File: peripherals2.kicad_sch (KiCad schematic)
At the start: 0 parts

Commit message: feat: adds the peripherals-2 to project
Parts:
- added C1, C2, C3: 0.1µF, symbol Device:C
- added J1: MSD-4-A, CUI_MSD-4-A, symbol MSD-4-A:MSD-4-A
- added R1, R2, R3, R4, R5, R6, R7, R8, R9: 10k, symbol Device:R
- added U1: GSDA213, LGA12_GAS, symbol GSDA213:GSDA213
- added U2: VEML3235SL, symbol VEML3235SL:BL0937
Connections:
- new net: R7.1, U2.3 (INT)
- new net: C3.2, U1.3 (VDD_IO)
- new net: R8.2, U1.5 (INT1)
- new net: R9.2, U1.6 (INT2)
- new net +3.3V: C1.2, C2.2, J1.1 (DAT2), J1.2 (CD/DAT3), J1.4 (VDD), J1.8 (DAT1), R1.1, R2.1, R3.1, R5.2, R6.2, R7.2, R8.1, R9.1, U1.7 (VDD), U2.1 (VDD), U2.4 (SDA), U2.5 (SCL)
- new net CS: U1.10 (CSB)
- new net GND: C1.1, C2.1, C3.1, J1.6 (VSS), J1.G1 (COVER_GND), J1.G2 (COVER_GND__1), J1.G3 (COVER_GND__2), J1.G4 (COVER_GND__3), R1.2, R2.2, R3.2, R4.2, R5.1, R6.1, U1.8 (GND_IO), U1.9 (GND), U2.2 (GND)
- new net GPIO: J1.CD, R4.1
- new net MISO: J1.7 (DAT0), U1.2 (SDA/SDI/SDO)
- new net MOSI: J1.3 (CMD), U1.1 (SDO/SA0)
- new net SCLK: J1.5 (CLK), U1.12 (SCL/SCLK)

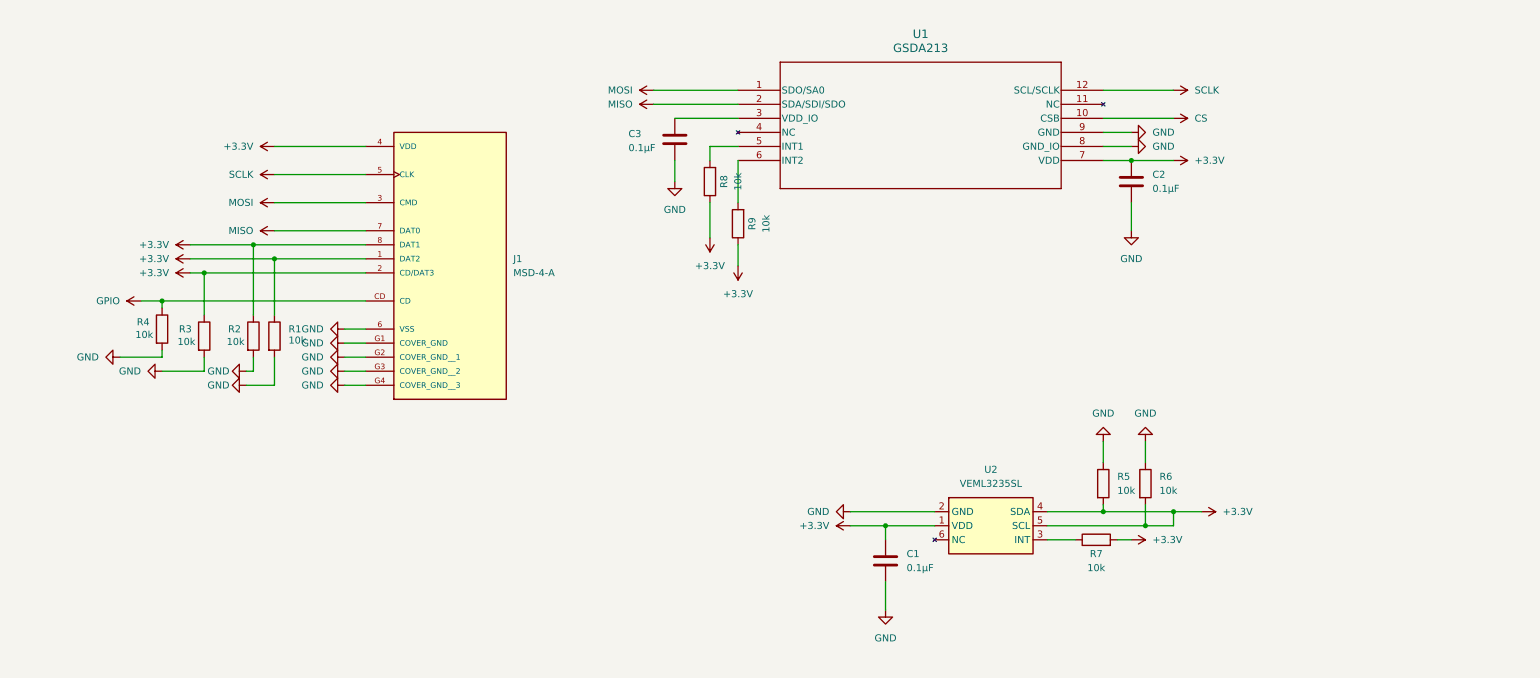
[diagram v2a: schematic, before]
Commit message: refac: adjusts circuits for MicroSD, Accelerometer, Light Sensor
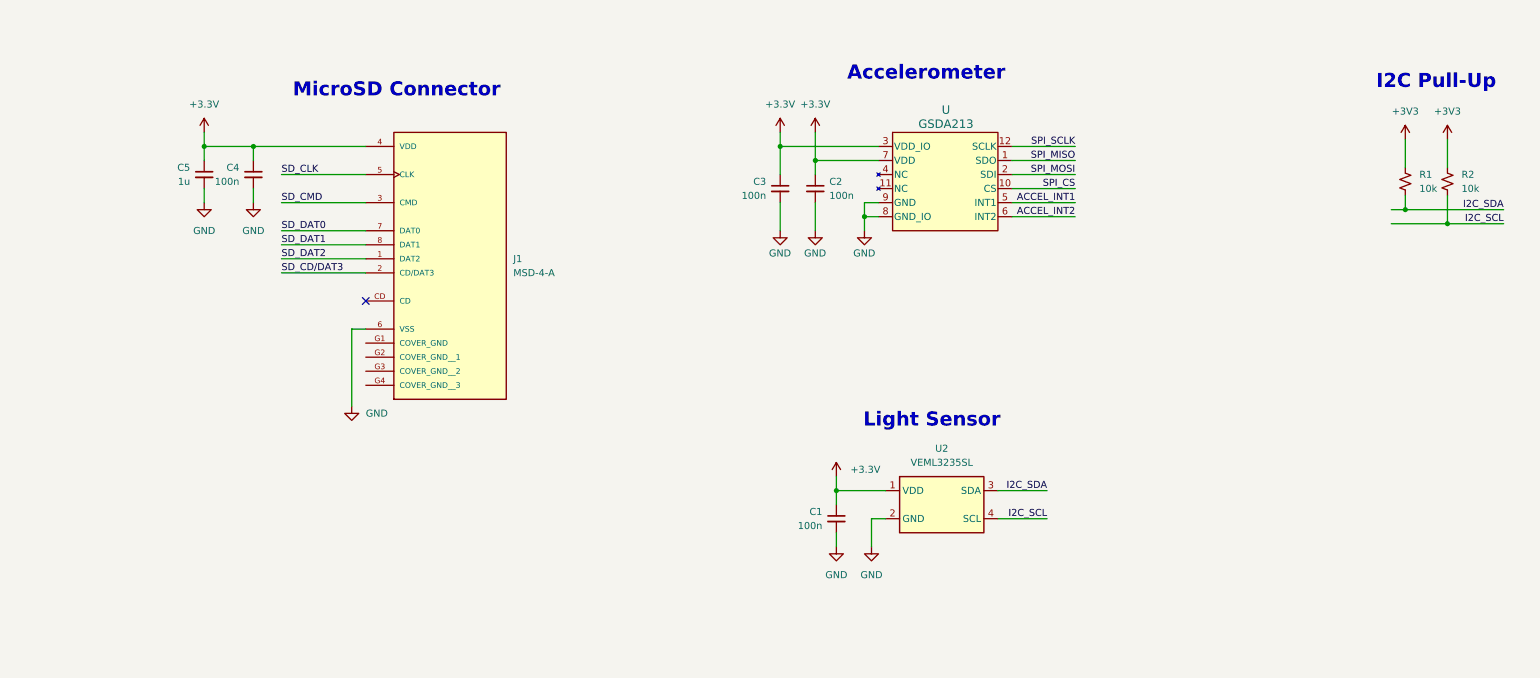
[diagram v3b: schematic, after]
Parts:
- removed C1, C2, C3: 0.1µF, symbol Device:C
- removed R1, R2, R3, R4, R5, R6, R7, R8, R9: 10k, symbol Device:R
- added C1, C2, C3, C4: 100n, symbol Device:C_Small
- added C5: 1u, Capacitor_SMD:C_0402_1005Metric, symbol Device:C_Small
- added R1, R2: 10k, Resistor_SMD:R_0402_1005Metric, symbol Device:R_Small_US
- U: renamed from U1; footprint LGA12_GAS -> (none); MPN (none) -> GSDA213
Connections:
- net +3.3V: now also U.3 (VDD_IO), C1.1, C2.1, C3.1, C4.1, C5.1; no longer J1.1 (DAT2), J1.2 (CD/DAT3), J1.8 (DAT1), U2.4 (SDA), U2.5 (SCL)
- net GND: now also C1.2, C2.2, C3.2, C4.2, C5.2; no longer J1.G1 (COVER_GND), J1.G2 (COVER_GND__1), J1.G3 (COVER_GND__2), J1.G4 (COVER_GND__3)
- net I2C_SDA: now reaches U2.3 (SDA)
- net I2C_SDA: now also R1.2
- net ACCEL_INT1: now reaches U.5 (INT1)
- net ACCEL_INT2: now reaches U.6 (INT2)
- net CS renamed SPI_CS
- net GPIO: no longer names the net of J1.CD
- net MISO renamed SD_DAT0
- net SD_DAT0: no longer U.2 (SDA/SDI/SDO)
- net MOSI renamed SD_CMD
- net SD_CMD: no longer U.1 (SDO/SA0)
- net SCLK renamed SD_CLK
- net SD_CLK: no longer U.12 (SCL/SCLK)
- new net +3V3: R1.1, R2.1
- new net I2C_SCL: R2.2, U2.4 (SCL)
- new net SD_CD/DAT3: J1.2 (CD/DAT3)
- new net SD_DAT1: J1.8 (DAT1)
- new net SD_DAT2: J1.1 (DAT2)
- new net SPI_MISO: U.1 (SDO)
- new net SPI_MOSI: U.2 (SDI)
- new net SPI_SCLK: U.12 (SCLK)
- no-connect marks 0 -> 1
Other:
- note added: "Accelerometer"
- note added: "I2C Pull-Up"
- note added: "Light Sensor"
- note added: "MicroSD Connector"

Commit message: fix: adds footprint to capacitors
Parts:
- C1, C2, C3, C4: footprint (none) -> Capacitor_SMD:C_0402_1005Metric
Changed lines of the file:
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@@
 			)
 		)
-		(property "Footprint" ""
+		(property "Footprint" "Capacitor_SMD:C_0402_1005Metric"
 			(at 160.02 45.72 0)
 			(effects
@@
 			)
 		)
-		(property "Footprint" ""
+		(property "Footprint" "Capacitor_SMD:C_0402_1005Metric"
 			(at 163.83 105.41 0)
 			(effects
@@
 			)
 		)
-		(property "Footprint" ""
+		(property "Footprint" "Capacitor_SMD:C_0402_1005Metric"
 			(at 58.42 43.18 0)
 			(effects
@@
 			)
 		)
-		(property "Footprint" ""
+		(property "Footprint" "Capacitor_SMD:C_0402_1005Metric"
 			(at 153.67 45.72 0)
 			(effects

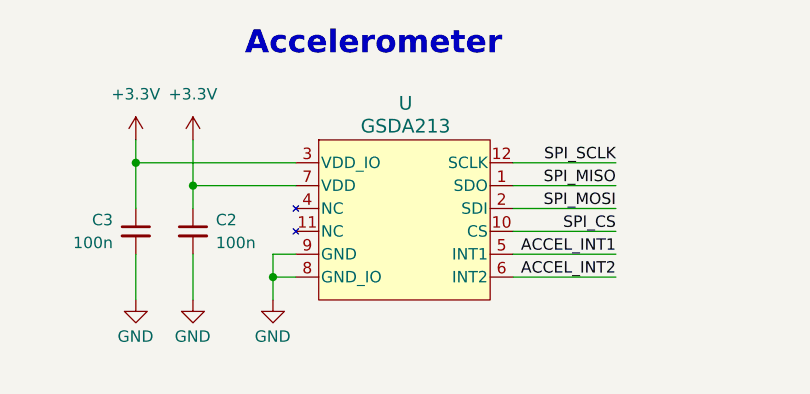
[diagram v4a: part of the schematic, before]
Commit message: fix: corrects accelerometer designator
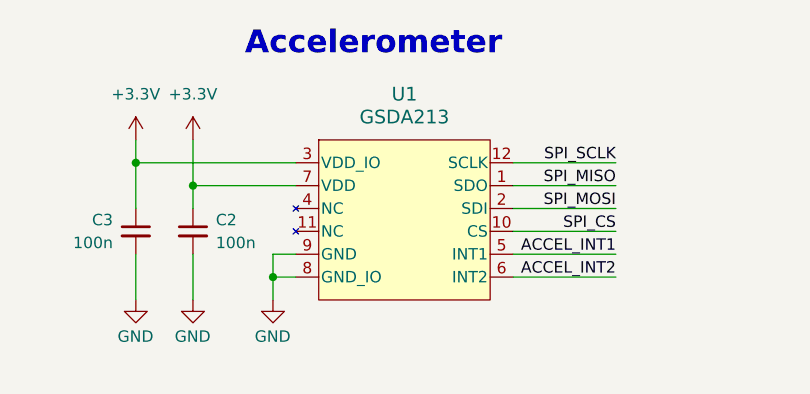
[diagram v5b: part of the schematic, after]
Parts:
- renumbered U to U1
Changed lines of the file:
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@@
 		(dnp no)
 		(fields_autoplaced yes)
-		(property "Reference" "U"
-			(at 183.642 31.496 0)
+		(property "Reference" "U1"
+			(at 183.515 30.48 0)
 			(effects
 				(font
@@
 		)
 		(property "Value" "GSDA213"
-			(at 183.642 34.036 0)
+			(at 183.515 33.02 0)
 			(effects
 				(font
@@
 			(project ""
 				(path "/b90666d0-8852-4bb1-832d-f9d855027372/e26c05ee-f364-47de-be04-e77902e037c8"
-					(reference "U")
+					(reference "U1")
 					(unit 1)
 				)

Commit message: refac: reannotates designators
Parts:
- renumbered C5 to C42, C4 to C43, C3 to C44, C2 to C45, C1 to C46, J1 to J4, R1 to R34, R2 to R35, U1 to U8, U2 to U9
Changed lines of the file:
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@@
 		(dnp no)
 		(fields_autoplaced yes)
-		(property "Reference" "J1"
+		(property "Reference" "J4"
 			(at 105.41 58.4199 0)
 			(effects
@@
 			(project ""
 				(path "/b90666d0-8852-4bb1-832d-f9d855027372/e26c05ee-f364-47de-be04-e77902e037c8"
-					(reference "J1")
+					(reference "J4")
 					(unit 1)
 				)
@@
 		(dnp no)
 		(fields_autoplaced yes)
-		(property "Reference" "#PWR027"
+		(property "Reference" "#PWR0126"
 			(at 163.83 101.6 0)
 			(effects
@@
 			(project "zbook"
 				(path "/b90666d0-8852-4bb1-832d-f9d855027372/e26c05ee-f364-47de-be04-e77902e037c8"
-					(reference "#PWR027")
+					(reference "#PWR0126")
 					(unit 1)
 				)
@@
 		(dnp no)
 		(fields_autoplaced yes)
-		(property "Reference" "#PWR05"
+		(property "Reference" "#PWR0116"
 			(at 153.67 39.37 0)
 			(effects
@@
 			(project "zbook"
 				(path "/b90666d0-8852-4bb1-832d-f9d855027372/e26c05ee-f364-47de-be04-e77902e037c8"
-					(reference "#PWR05")
+					(reference "#PWR0116")
 					(unit 1)
 				)
@@
 		(dnp no)
 		(fields_autoplaced yes)
-		(property "Reference" "#PWR09"
+		(property "Reference" "#PWR0119"
 			(at 274.32 40.64 0)
 			(effects
@@
 			(project "zbook"
 				(path "/b90666d0-8852-4bb1-832d-f9d855027372/e26c05ee-f364-47de-be04-e77902e037c8"
-					(reference "#PWR09")
+					(reference "#PWR0119")
 					(unit 1)
 				)
@@
 		(dnp no)
 		(fields_autoplaced yes)
-		(property "Reference" "#PWR08"
+		(property "Reference" "#PWR0118"
 			(at 266.7 40.64 0)
 			(effects
@@
 			(project "zbook"
 				(path "/b90666d0-8852-4bb1-832d-f9d855027372/e26c05ee-f364-47de-be04-e77902e037c8"
-					(reference "#PWR08")
+					(reference "#PWR0118")
 					(unit 1)
 				)
@@
 		(on_board yes)
 		(dnp no)
-		(property "Reference" "C2"
+		(property "Reference" "C45"
 			(at 162.56 44.4562 0)
 			(effects
@@
 			(project "zbook"
 				(path "/b90666d0-8852-4bb1-832d-f9d855027372/e26c05ee-f364-47de-be04-e77902e037c8"
-					(reference "C2")
+					(reference "C45")
 					(unit 1)
 				)
@@
 		(dnp no)
 		(fields_autoplaced yes)
-		(property "Reference" "U1"
+		(property "Reference" "U8"
 			(at 183.515 30.48 0)
 			(effects
@@
 			(project ""
 				(path "/b90666d0-8852-4bb1-832d-f9d855027372/e26c05ee-f364-47de-be04-e77902e037c8"
-					(reference "U1")
+					(reference "U8")
 					(unit 1)
 				)
@@
 		(dnp no)
 		(fields_autoplaced yes)
-		(property "Reference" "#PWR028"
+		(property "Reference" "#PWR0127"
 			(at 163.83 116.84 0)
 			(effects
@@
 			(project "zbook"
 				(path "/b90666d0-8852-4bb1-832d-f9d855027372/e26c05ee-f364-47de-be04-e77902e037c8"
-					(reference "#PWR028")
+					(reference "#PWR0127")
 					(unit 1)
 				)
@@
 		(dnp no)
 		(fields_autoplaced yes)
-		(property "Reference" "C1"
+		(property "Reference" "C46"
 			(at 161.29 104.1462 0)
 			(effects
@@
 			(project ""
 				(path "/b90666d0-8852-4bb1-832d-f9d855027372/e26c05ee-f364-47de-be04-e77902e037c8"
-					(reference "C1")
+					(reference "C46")
 					(unit 1)
 				)
@@
 		(dnp no)
 		(fields_autoplaced yes)
-		(property "Reference" "#PWR06"
+		(property "Reference" "#PWR0117"
 			(at 160.02 39.37 0)
 			(effects
@@
 			(project "zbook"
 				(path "/b90666d0-8852-4bb1-832d-f9d855027372/e26c05ee-f364-47de-be04-e77902e037c8"
-					(reference "#PWR06")
+					(reference "#PWR0117")
 					(unit 1)
 				)
@@
 		(dnp no)
 		(fields_autoplaced yes)
-		(property "Reference" "C4"
+		(property "Reference" "C43"
 			(at 55.88 41.9162 0)
 			(effects
@@
 			(project "zbook"
 				(path "/b90666d0-8852-4bb1-832d-f9d855027372/e26c05ee-f364-47de-be04-e77902e037c8"
-					(reference "C4")
+					(reference "C43")
 					(unit 1)
 				)
@@
 		(dnp no)
 		(fields_autoplaced yes)
-		(property "Reference" "C3"
+		(property "Reference" "C44"
 			(at 151.13 44.4562 0)
 			(effects
@@
 			(project "zbook"
 				(path "/b90666d0-8852-4bb1-832d-f9d855027372/e26c05ee-f364-47de-be04-e77902e037c8"
-					(reference "C3")
+					(reference "C44")
 					(unit 1)
 				)
@@
 		(dnp no)
 		(fields_autoplaced yes)
-		(property "Reference" "U2"
+		(property "Reference" "U9"
 			(at 182.88 92.71 0)
 			(effects
@@
 			(project ""
 				(path "/b90666d0-8852-4bb1-832d-f9d855027372/e26c05ee-f364-47de-be04-e77902e037c8"
-					(reference "U2")
+					(reference "U9")
 					(unit 1)
 				)
@@
 		(dnp no)
 		(fields_autoplaced yes)
-		(property "Reference" "R1"
+		(property "Reference" "R34"
 			(at 269.24 43.1799 0)
 			(effects
@@
 			(project "zbook"
 				(path "/b90666d0-8852-4bb1-832d-f9d855027372/e26c05ee-f364-47de-be04-e77902e037c8"
-					(reference "R1")
+					(reference "R34")
 					(unit 1)
 				)
@@
 		(on_board yes)
 		(dnp no)
-		(property "Reference" "#PWR02"
+		(property "Reference" "#PWR0124"
 			(at 168.91 59.69 0)
 			(effects
@@
 			(project "zbook"
 				(path "/b90666d0-8852-4bb1-832d-f9d855027372/e26c05ee-f364-47de-be04-e77902e037c8"
-					(reference "#PWR02")
+					(reference "#PWR0124")
 					(unit 1)
 				)
@@
 		(dnp no)
 		(fields_autoplaced yes)
-		(property "Reference" "R2"
+		(property "Reference" "R35"
 			(at 276.86 43.1799 0)
 			(effects
@@
 			(project "zbook"
 				(path "/b90666d0-8852-4bb1-832d-f9d855027372/e26c05ee-f364-47de-be04-e77902e037c8"
-					(reference "R2")
+					(reference "R35")
 					(unit 1)
 				)
@@
 		(dnp no)
 		(fields_autoplaced yes)
-		(property "Reference" "#PWR011"
+		(property "Reference" "#PWR0125"
 			(at 76.2 91.44 0)
 			(effects
@@
 			(project "zbook"
 				(path "/b90666d0-8852-4bb1-832d-f9d855027372/e26c05ee-f364-47de-be04-e77902e037c8"
-					(reference "#PWR011")
+					(reference "#PWR0125")
 					(unit 1)
 				)
@@
 		(dnp no)
 		(fields_autoplaced yes)
-		(property "Reference" "#PWR036"
+		(property "Reference" "#PWR0128"
 			(at 170.18 116.84 0)
 			(effects
@@
 			(project "zbook"
 				(path "/b90666d0-8852-4bb1-832d-f9d855027372/e26c05ee-f364-47de-be04-e77902e037c8"
-					(reference "#PWR036")
+					(reference "#PWR0128")
 					(unit 1)
 				)
@@
 		(on_board yes)
 		(dnp no)
-		(property "Reference" "#PWR03"
+		(property "Reference" "#PWR0122"
 			(at 153.67 59.69 0)
 			(effects
@@
 			(project "zbook"
 				(path "/b90666d0-8852-4bb1-832d-f9d855027372/e26c05ee-f364-47de-be04-e77902e037c8"
-					(reference "#PWR03")
+					(reference "#PWR0122")
 					(unit 1)
 				)
@@
 		(dnp no)
 		(fields_autoplaced yes)
-		(property "Reference" "#PWR01"
+		(property "Reference" "#PWR0121"
 			(at 58.42 54.61 0)
 			(effects
@@
 			(project "zbook"
 				(path "/b90666d0-8852-4bb1-832d-f9d855027372/e26c05ee-f364-47de-be04-e77902e037c8"
-					(reference "#PWR01")
+					(reference "#PWR0121")
 					(unit 1)
 				)
@@
 		(on_board yes)
 		(dnp no)
-		(property "Reference" "C5"
+		(property "Reference" "C42"
 			(at 46.99 41.9162 0)
 			(effects
@@
 			(project ""
 				(path "/b90666d0-8852-4bb1-832d-f9d855027372/e26c05ee-f364-47de-be04-e77902e037c8"
-					(reference "C5")
+					(reference "C42")
 					(unit 1)
 				)
@@
 		(dnp no)
 		(fields_autoplaced yes)
-		(property "Reference" "#PWR07"
+		(property "Reference" "#PWR0115"
 			(at 49.53 39.37 0)
 			(effects
@@
 			(project "zbook"
 				(path "/b90666d0-8852-4bb1-832d-f9d855027372/e26c05ee-f364-47de-be04-e77902e037c8"
-					(reference "#PWR07")
+					(reference "#PWR0115")
 					(unit 1)
 				)
@@
 		(on_board yes)
 		(dnp no)
-		(property "Reference" "#PWR04"
+		(property "Reference" "#PWR0123"
 			(at 160.02 59.69 0)
 			(effects
@@
 			(project "zbook"
 				(path "/b90666d0-8852-4bb1-832d-f9d855027372/e26c05ee-f364-47de-be04-e77902e037c8"
-					(reference "#PWR04")
+					(reference "#PWR0123")
 					(unit 1)
 				)
@@
 		(dnp no)
 		(fields_autoplaced yes)
-		(property "Reference" "#PWR010"
+		(property "Reference" "#PWR0120"
 			(at 49.53 54.61 0)
 			(effects
@@
 			(project "zbook"
 				(path "/b90666d0-8852-4bb1-832d-f9d855027372/e26c05ee-f364-47de-be04-e77902e037c8"
-					(reference "#PWR010")
-					(unit 1)
-				)
+					(reference "#PWR0120")
+					(unit 1)
+				)

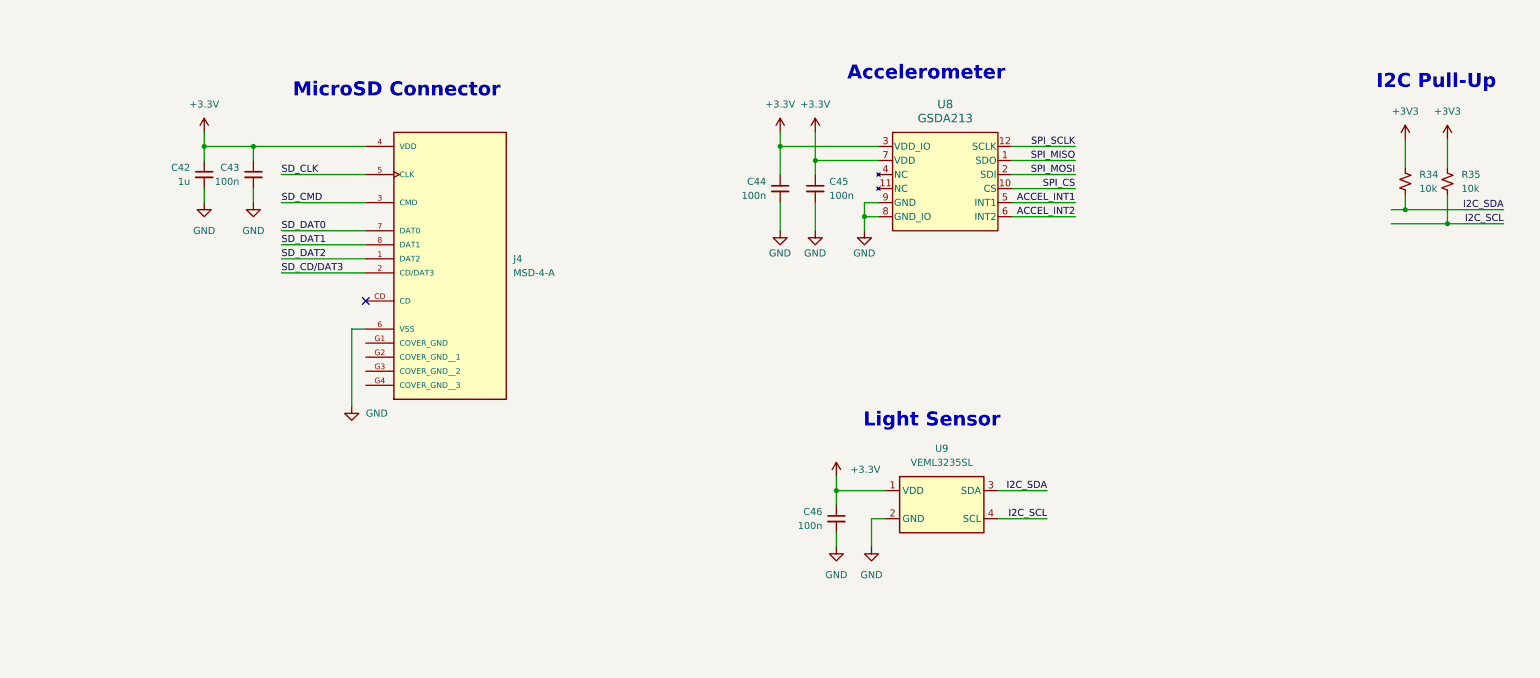
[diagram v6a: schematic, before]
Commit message: chore: links global labels
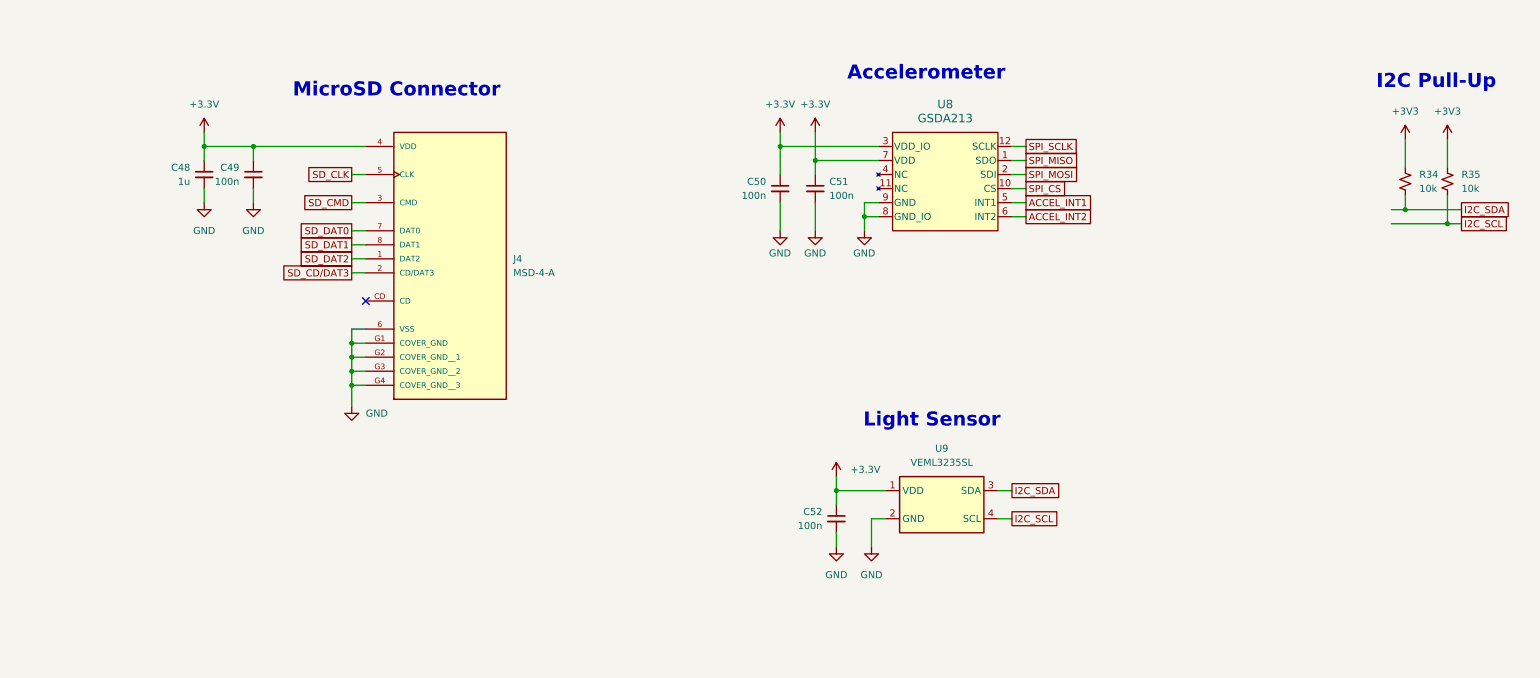
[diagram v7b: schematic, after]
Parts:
- renumbered C42 to C48, C43 to C49, C44 to C50, C45 to C51, C46 to C52
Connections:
- net GND: now also J4.G1 (COVER_GND), J4.G2 (COVER_GND__1), J4.G3 (COVER_GND__2), J4.G4 (COVER_GND__3)
